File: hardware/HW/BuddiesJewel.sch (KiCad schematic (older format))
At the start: 24 parts, among them CON1 AVR-ISP6, CON2 ANTENNE, IC1 ATTINY25-P, P1 ALIM, U1 PT, U2 PT, U3 PT, U4 PT, U5 RF430CL330H

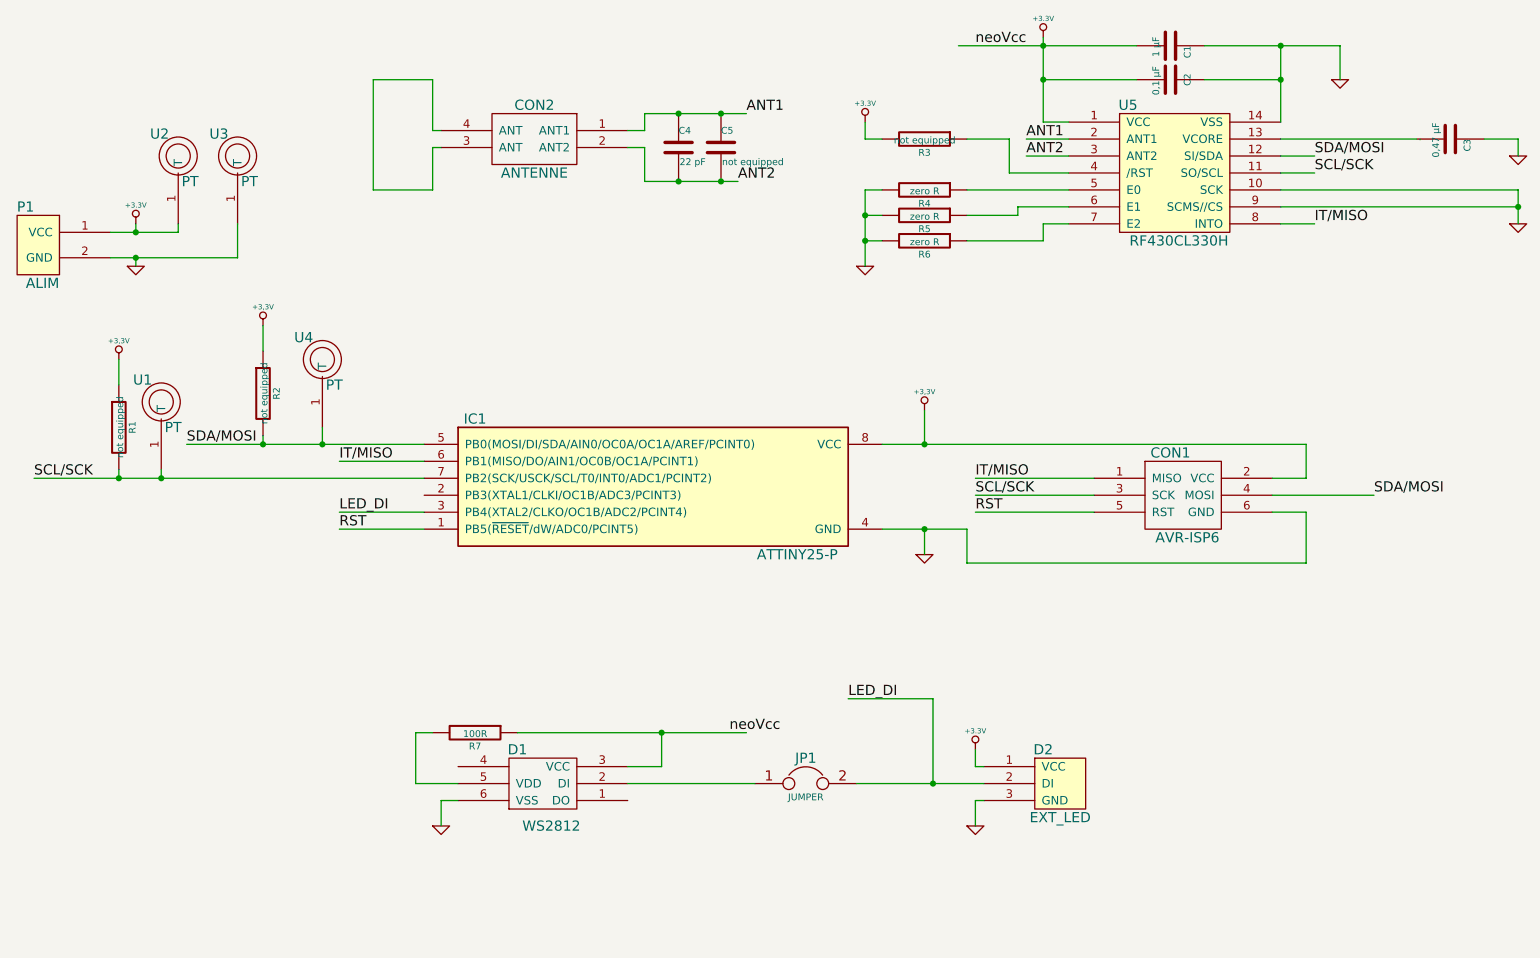
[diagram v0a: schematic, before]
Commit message: Use DIP footprint for TI chip Reroute to use 0,5mm nets
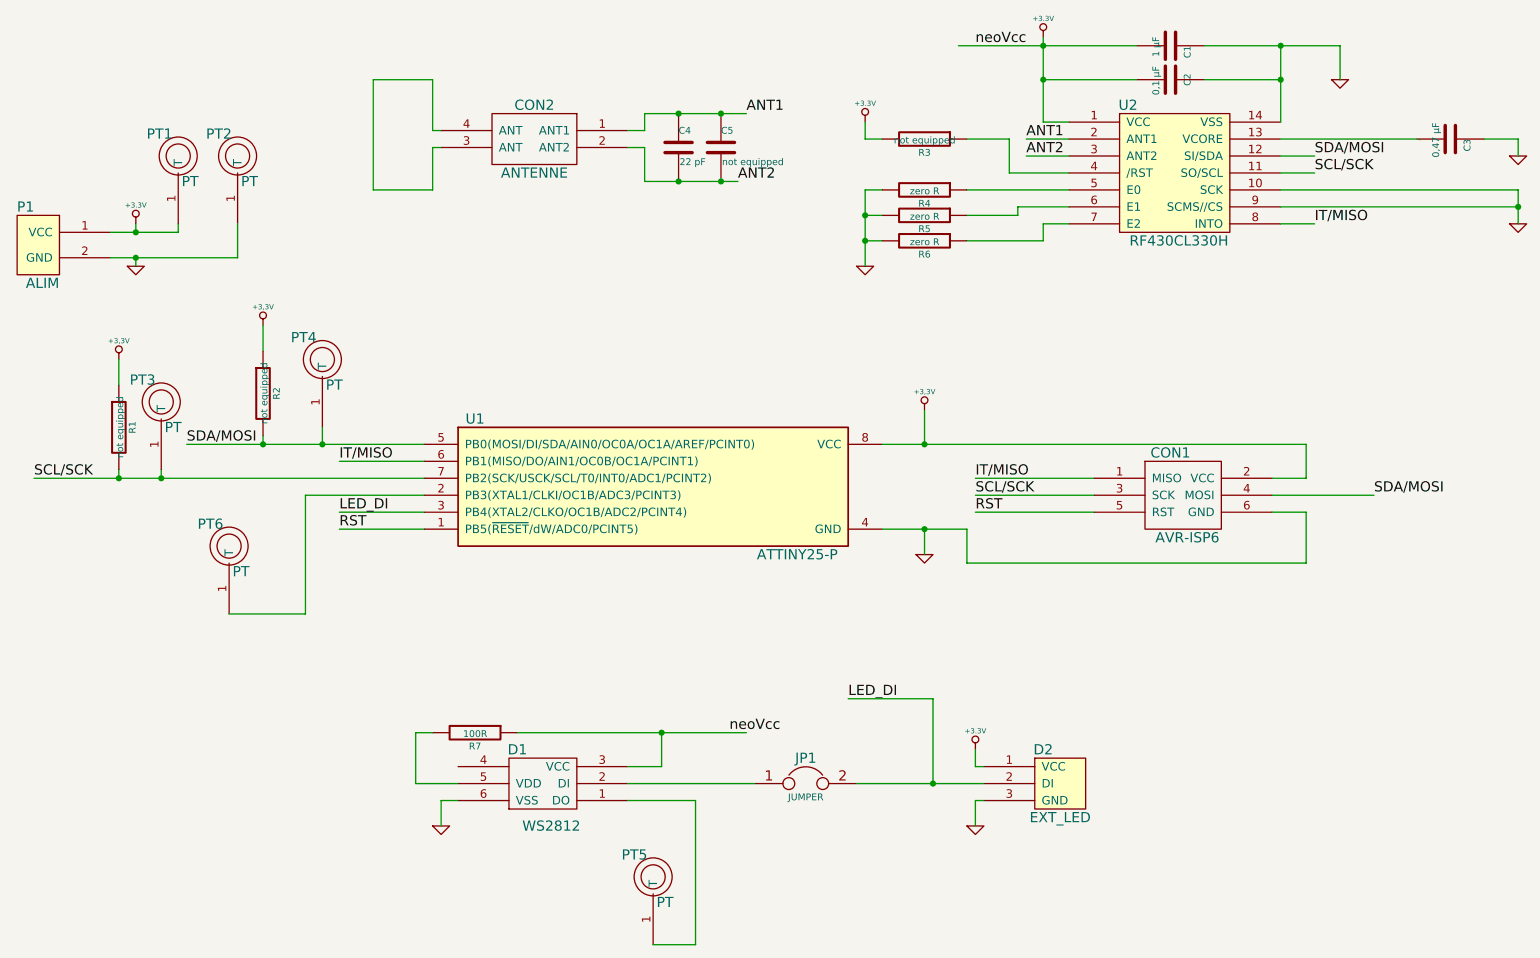
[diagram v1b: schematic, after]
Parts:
- added PT5, PT6: PT, ~, symbol PT
- renumbered U2 to PT1, U3 to PT2, U1 to PT3, U4 to PT4, IC1 to U1, U5 to U2
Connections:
- wire segments 96 -> 102
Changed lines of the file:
@@
 LIBS:BuddiesJewel-cache
 LIBS:BuddiesJewel-cache
-EELAYER 24 0
+EELAYER 27 0
 EELAYER END
 $Descr A4 11693 8268
@@
 Sheet 1 1
 Title "BuddiesJewel"
-Date "18 nov 2013"
+Date "1 dec 2013"
 Rev "1.2"
 Comp "FabLab"
@@
 $EndDescr
 $Comp
-L RF430CL330H U5
+L RF430CL330H U2
 U 1 1 5263BC72
 P 7850 1800
-F 0 "U5" H 7650 1750 60  0000 C CNN
+F 0 "U2" H 7650 1750 60  0000 C CNN
 F 1 "RF430CL330H" H 7950 950 60  0000 C CNN
 F 2 "~" H 7950 950 60  0000 C CNN
@@
 LED_DI
 $Comp
-L PT U2
+L PT PT1
 U 1 1 5283E30A
 P 2050 2200
-F 0 "U2" H 1940 2380 60  0000 C CNN
+F 0 "PT1" H 1940 2380 60  0000 C CNN
 F 1 "PT" H 2120 2100 60  0000 C CNN
 F 2 "~" H 1750 2450 60  0000 C CNN
@@
 $EndComp
 $Comp
-L PT U3
+L PT PT2
 U 1 1 5283E319
 P 2400 2200
-F 0 "U3" H 2290 2380 60  0000 C CNN
+F 0 "PT2" H 2290 2380 60  0000 C CNN
 F 1 "PT" H 2470 2100 60  0000 C CNN
 F 2 "~" H 2100 2450 60  0000 C CNN
@@
 $EndComp
 $Comp
-L ATTINY25-P IC1
+L ATTINY25-P U1
 U 1 1 5283EF71
 P 4850 4100
-F 0 "IC1" H 3800 4500 60  0000 C CNN
+F 0 "U1" H 3800 4500 60  0000 C CNN
 F 1 "ATTINY25-P" H 5700 3700 60  0000 C CNN
 F 2 "DIP8" H 3800 3700 60  0001 C CNN
@@
 $EndComp
 $Comp
-L PT U1
+L PT PT3
 U 1 1 5283F22D
 P 1950 3650
-F 0 "U1" H 1840 3830 60  0000 C CNN
+F 0 "PT3" H 1840 3830 60  0000 C CNN
 F 1 "PT" H 2020 3550 60  0000 C CNN
 F 2 "~" H 1650 3900 60  0000 C CNN
@@
 $EndComp
 $Comp
-L PT U4
+L PT PT4
 U 1 1 5283F23C
 P 2900 3400
-F 0 "U4" H 2790 3580 60  0000 C CNN
+F 0 "PT4" H 2790 3580 60  0000 C CNN
 F 1 "PT" H 2970 3300 60  0000 C CNN
 F 2 "~" H 2600 3650 60  0000 C CNN
@@
 Wire Wire Line
 	3550 5550 3450 5550
+$Comp
+L PT PT5
+U 1 1 529B82DD
+P 4850 6450
+F 0 "PT5" H 4740 6630 60  0000 C CNN
+F 1 "PT" H 4920 6350 60  0000 C CNN
+F 2 "~" H 4550 6700 60  0000 C CNN
+F 3 "~" H 4550 6700 60  0000 C CNN
+	1    4850 6450
+	1    0    0    -1
+$EndComp
+Wire Wire Line
+	4700 5950 5100 5950
+Wire Wire Line
+	5100 5950 5100 6800
+Wire Wire Line
+	5100 6800 4850 6800
+$Comp
+L PT PT6
+U 1 1 529B89E6
+P 2350 4500
+F 0 "PT6" H 2240 4680 60  0000 C CNN
+F 1 "PT" H 2420 4400 60  0000 C CNN
+F 2 "~" H 2050 4750 60  0000 C CNN
+F 3 "~" H 2050 4750 60  0000 C CNN
+	1    2350 4500
+	1    0    0    -1
+$EndComp
+Wire Wire Line
+	3500 4150 2800 4150
+Wire Wire Line
+	2800 4150 2800 4850
+Wire Wire Line
+	2800 4850 2350 4850
 $EndSCHEMATC

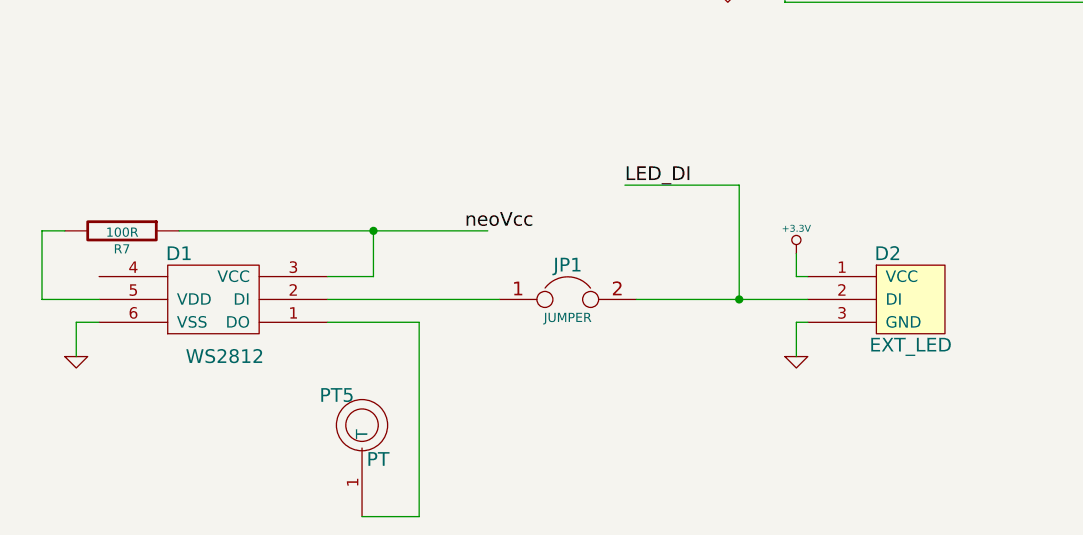
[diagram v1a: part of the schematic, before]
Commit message: PCB_v1.4
**will be used for our first etch**

- increase track width to .8mm (antenna tracks still in .5mm)
- remove the LED_DI jumper then replaced with a 0 ohm resistor (freed space)
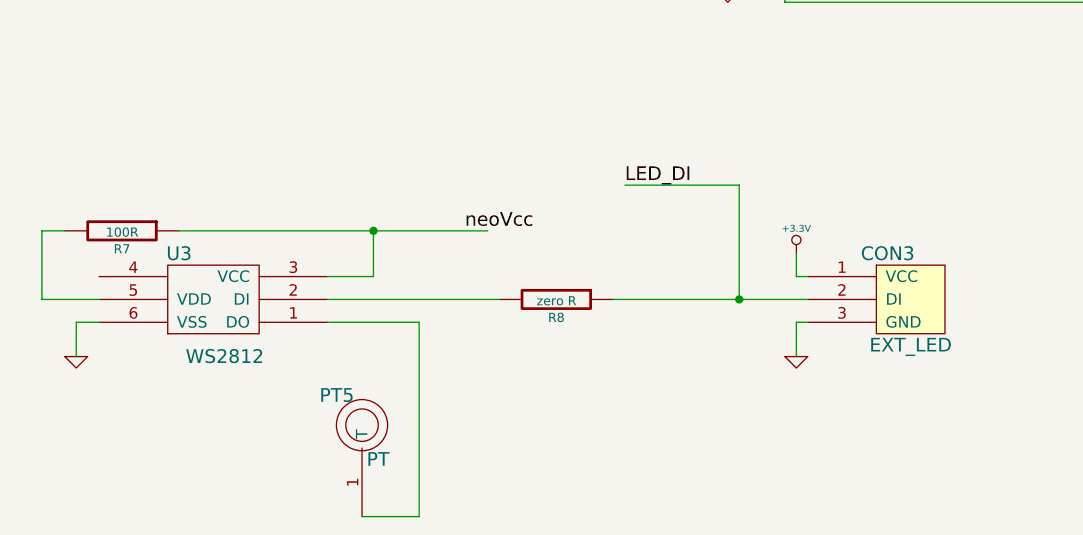
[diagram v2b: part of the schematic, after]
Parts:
- removed JP1: JUMPER, ~, symbol JUMPER
- added R8: zero R, ~, symbol R
- renumbered D2 to CON3, D1 to U3
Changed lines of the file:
@@
 encoding utf-8
 Sheet 1 1
-Title "BuddiesJewel"
-Date "1 dec 2013"
-Rev "1.2"
-Comp "FabLab"
+Title "Schema Proto BuddiesJewel"
+Date "3 dec 2013"
+Rev "1.4"
+Comp "BuddiesProjects"
 Comment1 ""
 Comment2 ""
@@
 $EndComp
 $Comp
-L JUMPER JP1
-U 1 1 5283EA50
-P 5750 5850
-F 0 "JP1" H 5750 6000 60  0000 C CNN
-F 1 "JUMPER" H 5750 5770 40  0000 C CNN
-F 2 "~" H 5750 5850 60  0000 C CNN
-F 3 "~" H 5750 5850 60  0000 C CNN
-	1    5750 5850
-	1    0    0    -1
-$EndComp
-$Comp
-L WS2812 D1
+L WS2812 U3
 U 1 1 5283EC88
 P 4150 5600
-F 0 "D1" H 4050 5550 60  0000 C CNN
+F 0 "U3" H 4050 5550 60  0000 C CNN
 F 1 "WS2812" H 4250 5100 60  0000 C CNN
 F 2 "~" H 4250 5100 60  0000 C CNN
@@
 	2400 2750 2400 2550
 Wire Wire Line
-	6050 5850 6800 5850
+	5950 5850 6800 5850
 Wire Wire Line
 	6500 5850 6500 5350
@@
 $EndComp
 $Comp
-L EXT_LED D2
+L EXT_LED CON3
 U 1 1 528A5C24
 P 7250 5650
-F 0 "D2" H 7150 5650 60  0000 C CNN
+F 0 "CON3" H 7150 5650 60  0000 C CNN
 F 1 "EXT_LED" H 7250 5250 60  0000 C CNN
 F 2 "~" H 7150 5650 60  0000 C CNN
@@
 Wire Wire Line
 	2800 4850 2350 4850
+$Comp
+L R R8
+U 1 1 529D238F
+P 5700 5850
+F 0 "R8" V 5780 5850 40  0000 C CNN
+F 1 "zero R" V 5707 5851 40  0000 C CNN
+F 2 "~" V 5630 5850 30  0000 C CNN
+F 3 "~" H 5700 5850 30  0000 C CNN
+	1    5700 5850
+	0    1    1    0
+$EndComp
 $EndSCHEMATC
